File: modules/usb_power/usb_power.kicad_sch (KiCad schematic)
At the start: 11 parts, among them J1 USB_C_Receptacle_PowerOnly_6P

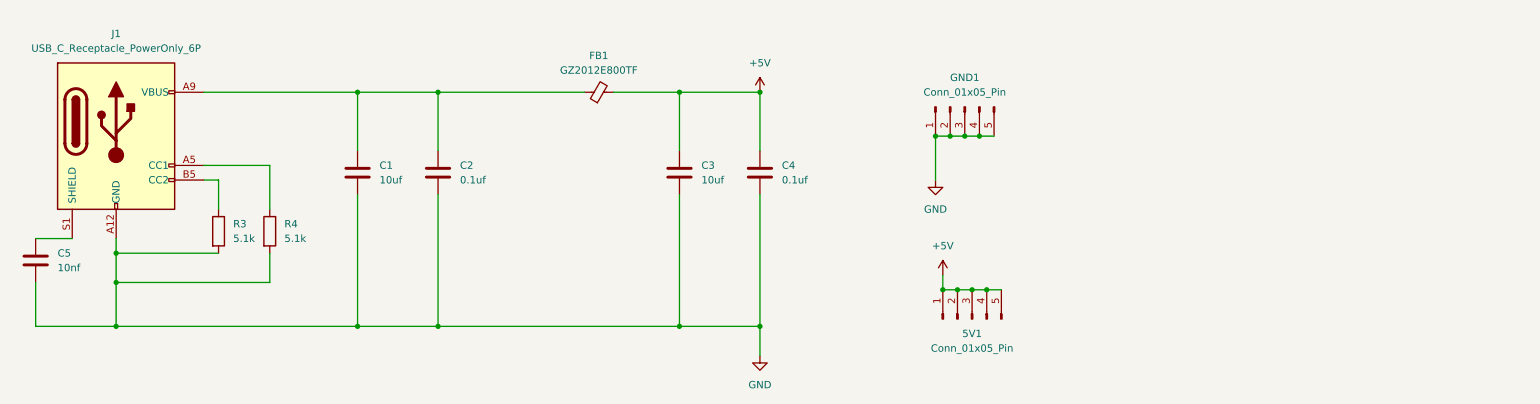
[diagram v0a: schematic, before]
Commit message: Update usb_power to regulate as 3.3V
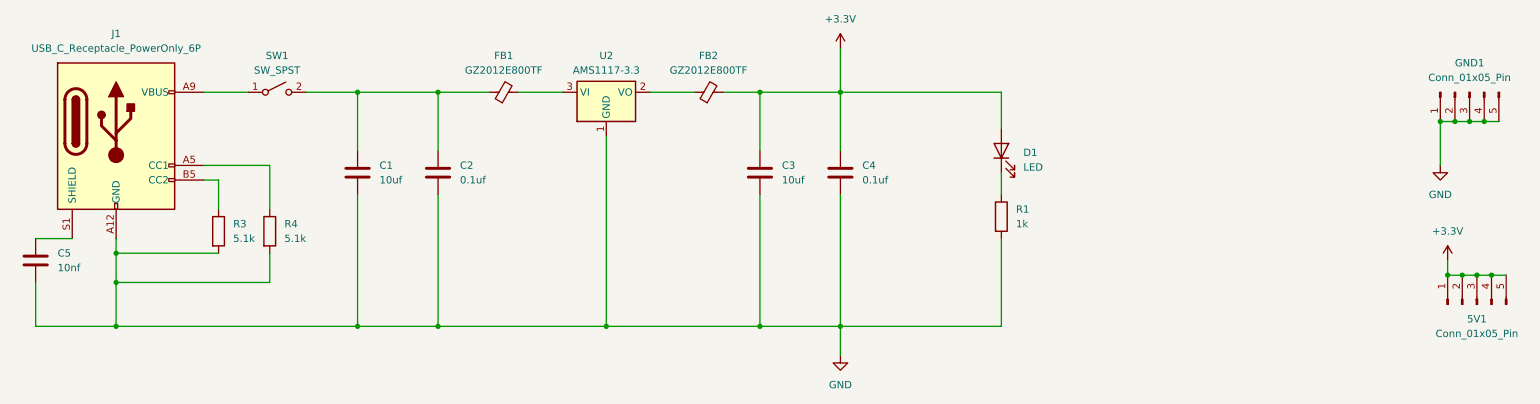
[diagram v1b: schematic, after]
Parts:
- added D1: LED, LED_SMD:LED_0603_1608Metric, symbol Device:LED
- added FB2: GZ2012E800TF, Capacitor_SMD:C_0805_2012Metric, symbol Device:FerriteBead_Small
- added R1: 1k, Resistor_SMD:R_0402_1005Metric, symbol Device:R
- added SW1: SW_SPST, BreadModular_MISC:SPST_TS-1187A-B-A-B, symbol Switch:SW_SPST
- added U2: AMS1117-3.3, Package_TO_SOT_SMD:SOT-223, symbol Regulator_Linear:AMS1117-3.3
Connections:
- net GND: now also R1.2, U2.1 (GND)
- net at C1.1, C2.1, FB1.1: now also SW1.2 (B); no longer J1.A9 (VBUS), J1.B9 (VBUS)
- net +5V renamed +3.3V
- net +3.3V: now also D1.2 (A), FB2.2; no longer FB1.2
- new net: FB2.1, U2.2 (VO)
- new net: D1.1 (K), R1.1
- new net: FB1.2, U2.3 (VI)
- new net: J1.A9 (VBUS), J1.B9 (VBUS), SW1.1 (A)
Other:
- moved on the sheet: 5V1, C3, C4, FB1, GND1

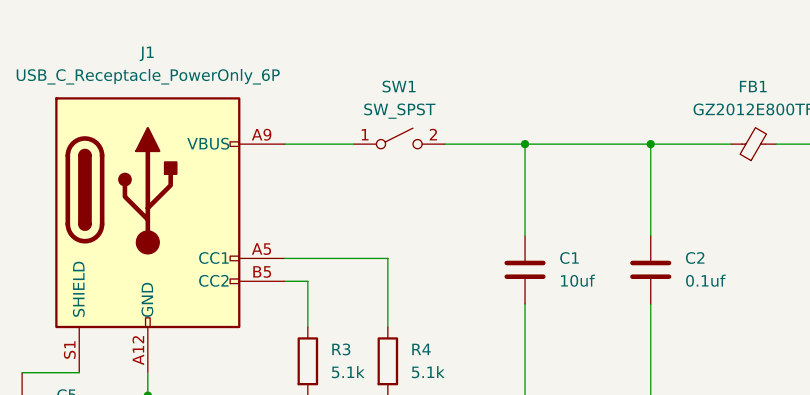
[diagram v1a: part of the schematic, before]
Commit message: Removed the usb_power tactile switch
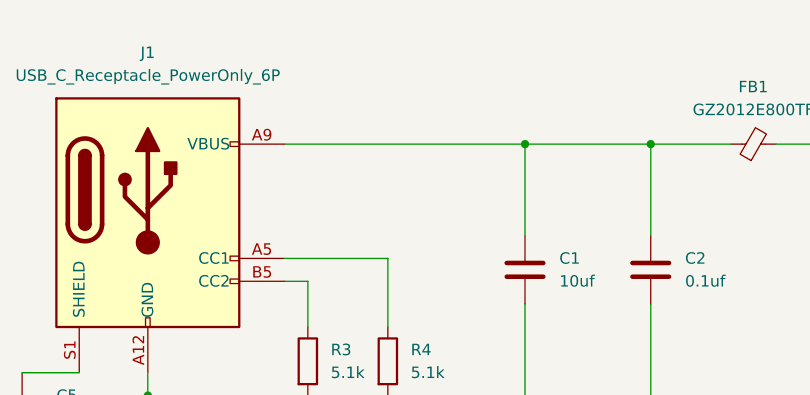
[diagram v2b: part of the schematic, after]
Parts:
- removed SW1: SW_SPST, BreadModular_MISC:SPST_TS-1187A-B-A-B, symbol Switch:SW_SPST
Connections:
- net at C1.1, C2.1, FB1.1: now also J1.A9 (VBUS), J1.B9 (VBUS)
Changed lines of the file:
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@@
-	(wire
-		(pts
-			(xy 76.2 35.56) (xy 67.31 35.56)
-		)
-		(stroke
-			(width 0)
-			(type default)
-		)
-	)
 	(wire
 		(pts
@@
 	(wire
 		(pts
-			(xy 57.15 35.56) (xy 49.53 35.56)
+			(xy 49.53 35.56) (xy 76.2 35.56)
 		)
 		(stroke
@@
 					(unit 1)
 				)
-			)
-		)
-	)
-	(symbol
-		(lib_id "Switch:SW_SPST")
-		(at 62.23 35.56 0)
-		(unit 1)
-		(exclude_from_sim no)
-		(in_bom yes)
-		(on_board yes)
-		(dnp no)
-		(fields_autoplaced yes)
-		(property "Reference" "SW1"
-			(at 62.23 29.21 0)
-			(effects
-				(font
-					(size 1.27 1.27)
-				)
-			)
-		)
-		(property "Value" "SW_SPST"
-			(at 62.23 31.75 0)
-			(effects
-				(font
-					(size 1.27 1.27)
-				)
-			)
-		)
-		(property "Footprint" "BreadModular_MISC:SPST_TS-1187A-B-A-B"
-			(at 62.23 35.56 0)
-			(effects
-				(font
-					(size 1.27 1.27)
-				)
-				(hide yes)
-			)
-		)
-		(property "Datasheet" "~"
-			(at 62.23 35.56 0)
-			(effects
-				(font
-					(size 1.27 1.27)
-				)
-				(hide yes)
-			)
-		)
-		(property "Description" "Single Pole Single Throw (SPST) switch"
-			(at 62.23 35.56 0)
-			(effects
-				(font
-					(size 1.27 1.27)
-				)
-				(hide yes)
-			)
-		)
-		(pin "1"
-		)
-		(pin "2"
-		)
-		(instances
-			(project ""
-				(path "/b63493d3-5f6d-47e3-845b-87e7090fc1ab"
-					(reference "SW1")
-					(unit 1)
-				)
